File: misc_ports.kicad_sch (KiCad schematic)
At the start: 36 parts, among them J10 685119134923, J27 USB Blaster JTAG, J28 UART, J29 MEGA65 Keyboard, J3 Wuerth_7499010121A, J30 Keyboard JTAG header, J7 QMTECH JTAG, J8 RTC, J9 1140084168 microSD Card Slot, P1 Full-side CD Card Slot, U12 DP83826, U13 74LVC374, U14 PTN3363BSMP

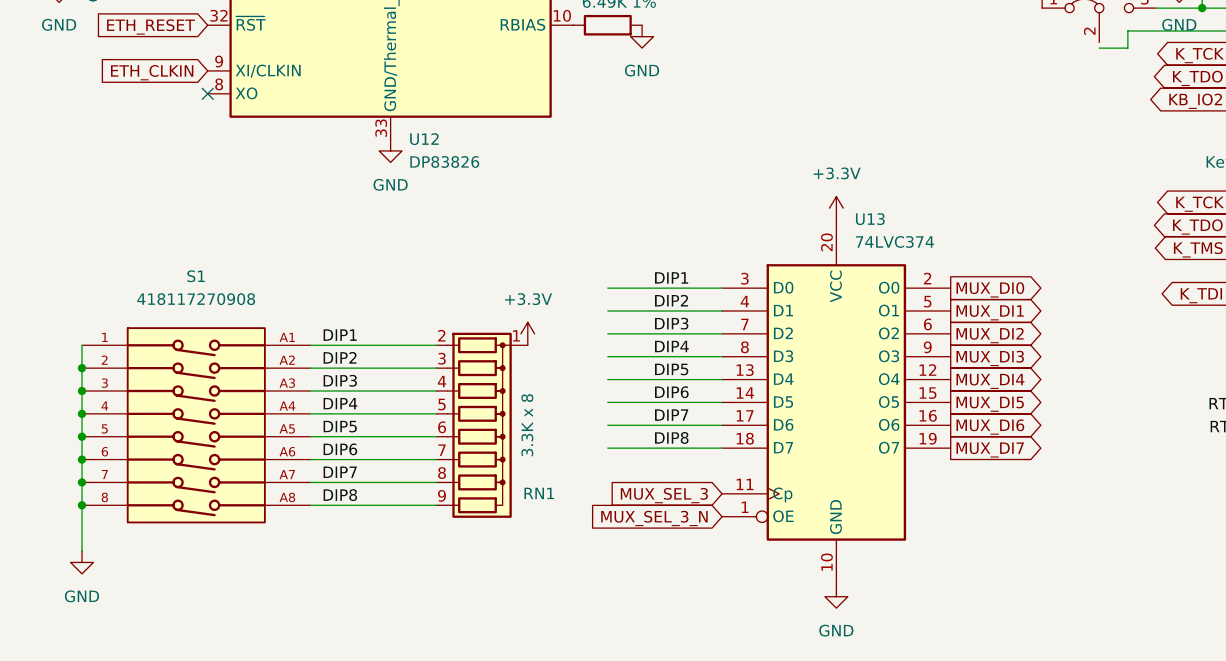
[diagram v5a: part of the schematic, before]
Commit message: switch DIP8 to DIP4 using spare pins on floppy MUX R unit
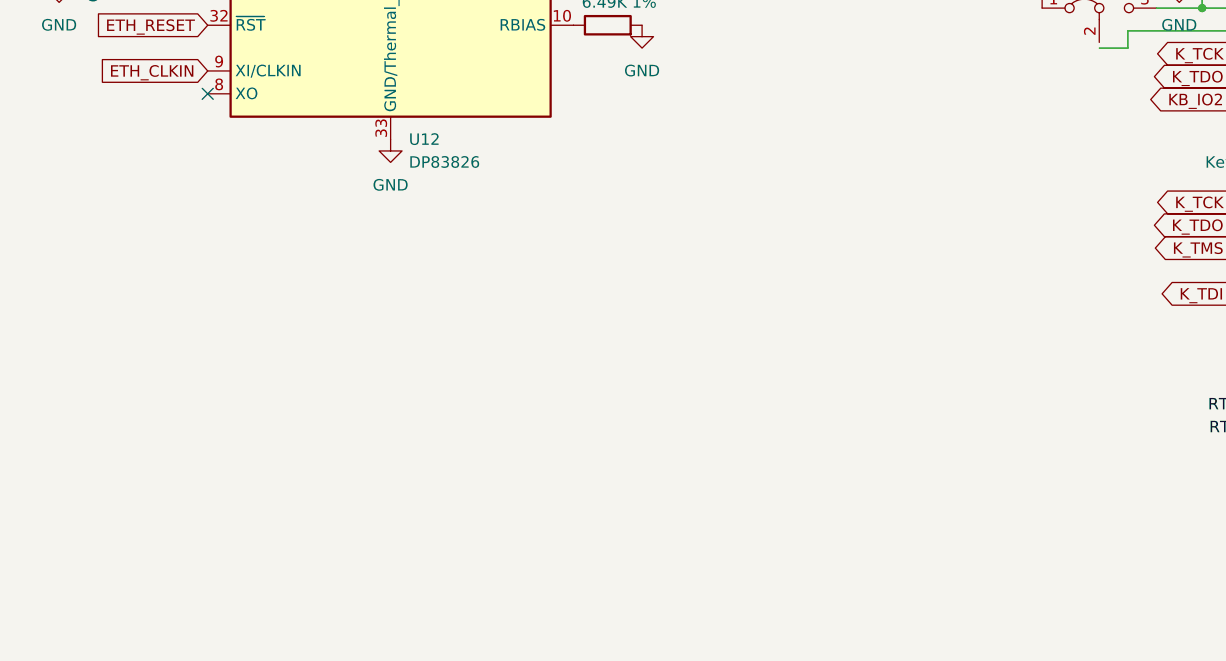
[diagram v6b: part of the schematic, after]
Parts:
- removed RN1: 3.3K x 8, Resistor_THT:R_Array_SIP9, symbol Device:R_Network08
- removed S1: 418117270908, snapeda:418117270908, symbol 00Project-DIP-Switch:418117270908
- removed U13: 74LVC374, Package_DIP:DIP-20_W7.62mm, symbol 74xx:74HC374

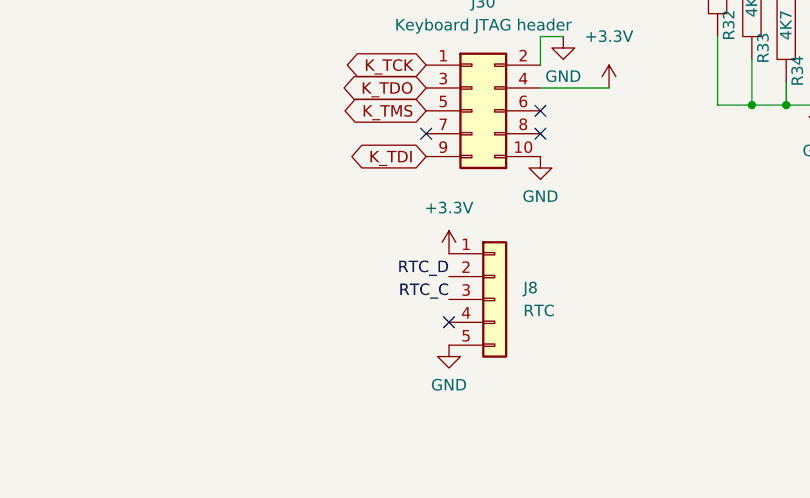
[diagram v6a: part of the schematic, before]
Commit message: relocate pins to connect RTC I2C
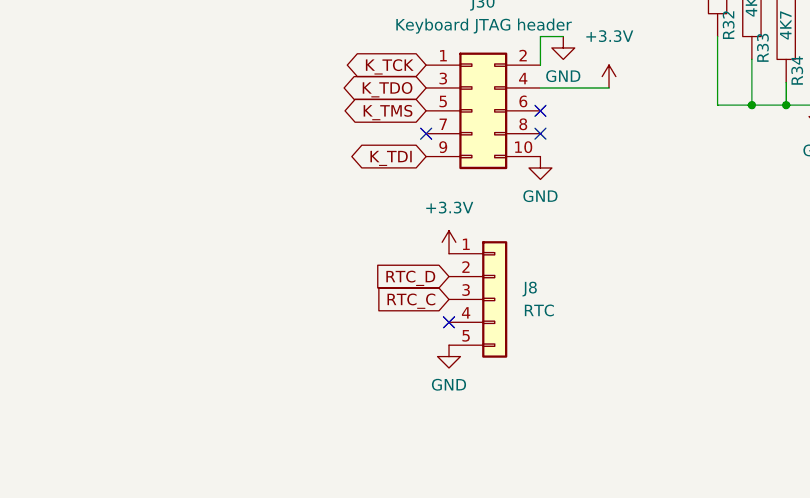
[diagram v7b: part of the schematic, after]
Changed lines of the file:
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@@
     (effects (font (size 1.27 1.27)) (justify left bottom))
-  )
-  (label "RTC_D" (at 148.59 171.45 180)
-    (effects (font (size 1.27 1.27)) (justify right bottom))
   )
   (label "SCL_B" (at 247.65 139.7 180)
@@
     (effects (font (size 1.27 1.27)) (justify left bottom))
   )
-  (label "RTC_C" (at 148.59 173.99 180)
-    (effects (font (size 1.27 1.27)) (justify right bottom))
-  )
   (label "D0+" (at 247.65 119.38 180)
     (effects (font (size 1.27 1.27)) (justify right bottom))
@@
     )
   )
+  (global_label "RTC_D" (shape input) (at 148.59 171.45 180) (fields_autoplaced)
+    (effects (font (size 1.27 1.27)) (justify right))
+    (property "Intersheet References" "${INTERSHEET_REFS}" (id 0) (at 140.4317 171.3706 0)
+      (effects (font (size 1.27 1.27)) (justify right) hide)
+    )
+  )
   (global_label "JTAG_TCK" (shape bidirectional) (at 255.905 20.955 180) (fields_autoplaced)
     (effects (font (size 1.27 1.27)) (justify right))
@@
       (effects (font (size 1.27 1.27)) (justify right) hide)
     )
+  )
+  (global_label "RTC_C" (shape input) (at 148.59 173.99 180) (fields_autoplaced)
+    (effects (font (size 1.27 1.27)) (justify right))
+    (property "Intersheet References" "${INTERSHEET_REFS}" (id 0) (at 140.4317 173.9106 0)
+      (effects (font (size 1.27 1.27)) (justify right) hide)
+    )
